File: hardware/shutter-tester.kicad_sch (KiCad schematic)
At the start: 17 parts, among them J1 Conn_01x05_Pin, U1 ESP32-C3_SUPERMINI, U2 Sensor-1, U3 Sensor-3, U4 Sensor-2

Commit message: v2.0 of the hardware
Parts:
- removed J1: Conn_01x05_Pin, Connector_PinHeader_2.54mm:PinHeader_1x05_P2.54mm_Vertical, symbol Connector:Conn_01x05_Pin
- C1, C2, C3: value C -> 0.01uF
- R4, R6, R8: value 2k -> 1k
- R5, R7, R9: value 1k -> 2k
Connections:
- net +5V: now also C1.2, C2.1, C3.2
- net GND: now also C2.2; no longer C2.1
- net SENSOR_1: now also U1.0 (GPIO0); no longer U1.2 (GPIO2)
- net SENSOR_2: now also U1.21 (GPIO21); no longer U1.3 (GPIO3)
- net SENSOR_3: now also U1.20 (GPIO20); no longer U1.4 (GPIO4)
- net at R3.2, R8.2, U3.2 (OUT): no longer C3.2
- net at R1.2, R4.2, U2.2 (OUT): no longer C1.2
- net at R2.2, R6.2, U4.2 (OUT): no longer C2.2
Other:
- moved on the sheet: C1, C2, C3, R2, R3, R6, R7, R8, R9, U3, U4

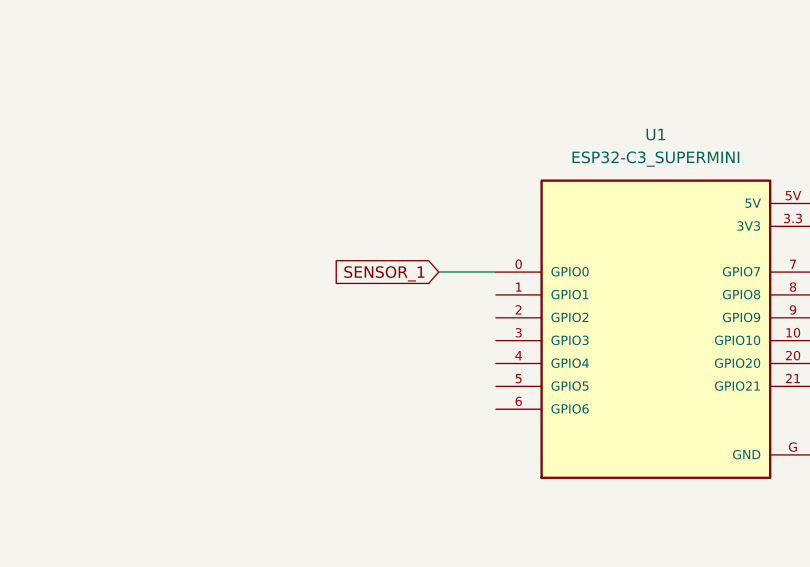
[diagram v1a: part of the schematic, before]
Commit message: Don't use GPIO 0 for sensor input
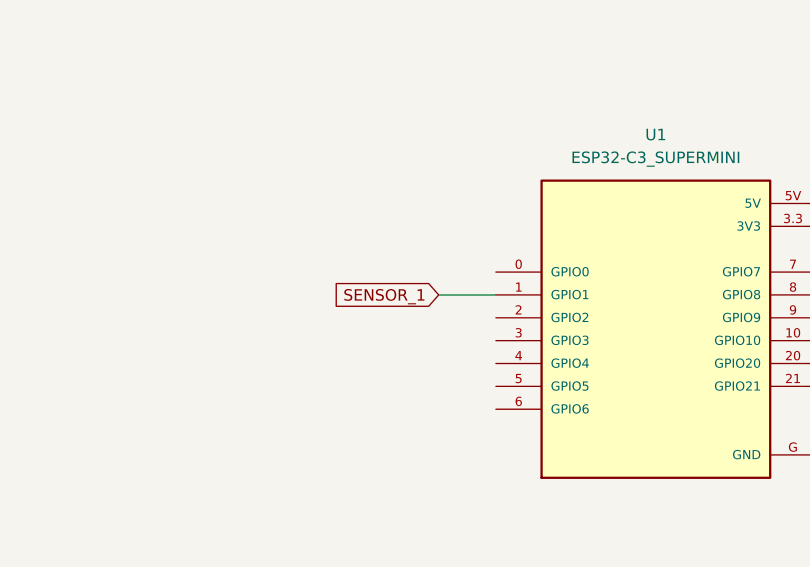
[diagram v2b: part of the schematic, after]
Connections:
- net SENSOR_1: now also U1.1 (GPIO1); no longer U1.0 (GPIO0)
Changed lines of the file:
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@@
+	(wire
+		(pts
+			(xy 100.33 95.25) (xy 106.68 95.25)
+		)
+		(stroke
+			(width 0)
+			(type default)
+		)
+	)
 	(wire
 		(pts
@@
 		(pts
 			(xy 146.05 38.1) (xy 151.13 38.1)
-		)
-		(stroke
-			(width 0)
-			(type default)
-		)
-	)
-	(wire
-		(pts
-			(xy 100.33 92.71) (xy 106.68 92.71)
 		)
 		(stroke
@@
 	(global_label "SENSOR_1"
 		(shape input)
-		(at 100.33 92.71 180)
+		(at 100.33 95.25 180)
 		(fields_autoplaced yes)
 		(effects
@@
 		)
 		(property "Intersheetrefs" "${INTERSHEET_REFS}"
-			(at 87.6687 92.71 0)
+			(at 87.6687 95.25 0)
 			(effects
 				(font
